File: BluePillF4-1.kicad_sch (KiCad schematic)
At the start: 57 parts, among them J1 MH20-1, J2 MH20-1, J3 MH_RA4-1, J4 47309-2651, J5 U02-BFD3111B0-009, U3 STM32F405RGT6, U4 SY6280, Y1 FC-12M, Y2 NX3225GD

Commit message: Removed unnecessary components like LiPo charger and fixed most errors. First connections between LoRa module and MCU created in the schematic.
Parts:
- removed R20: 0R, BluePillF4 Lib:R0603, symbol BluePillF4:RES_0603
- removed R21, R22: 10k, BluePillF4 Lib:R0603, symbol BluePillF4:RES_0603
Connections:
- net +VBAT is gone; now on net +3V3: J3.4
- net +3V3: now also J2.1
- net +3V3A: no longer J2.1
- net PA4 renamed LoRa_NSS
- net PA5 renamed LoRa_SCK
- net PA6 renamed LoRa_MISO
- net PA7 renamed LoRa_MOSI
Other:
- note removed: "Note: Mount L1 or U2, but not both"
- note removed: "VOLTAGE SENSE"

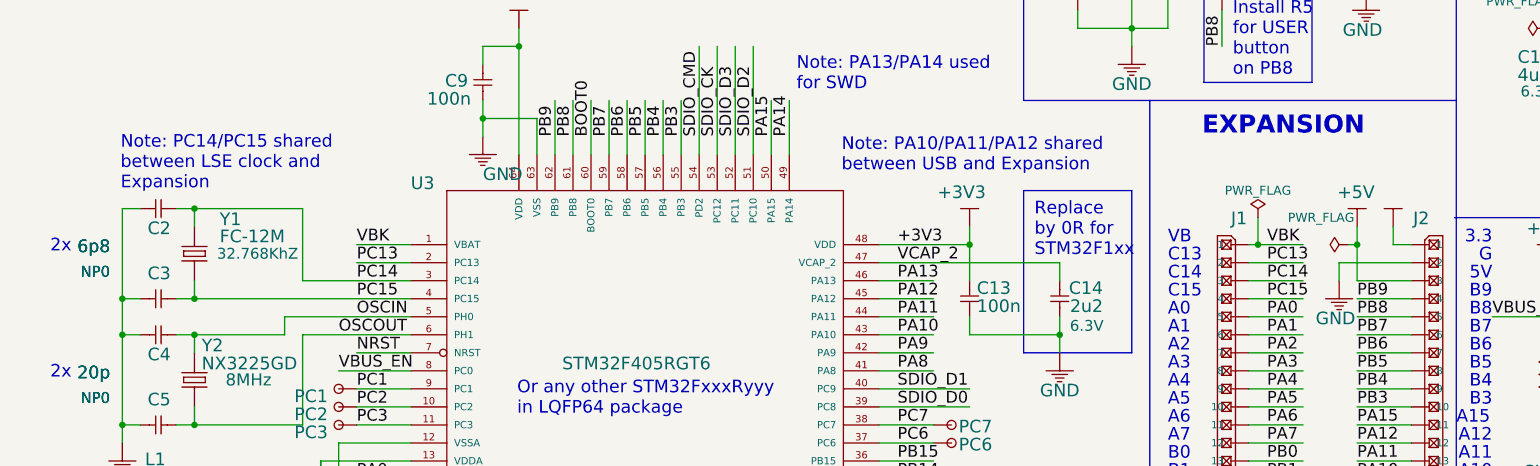
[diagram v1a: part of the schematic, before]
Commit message: Delete the RTC oscillator. First routing of the LoRa module.
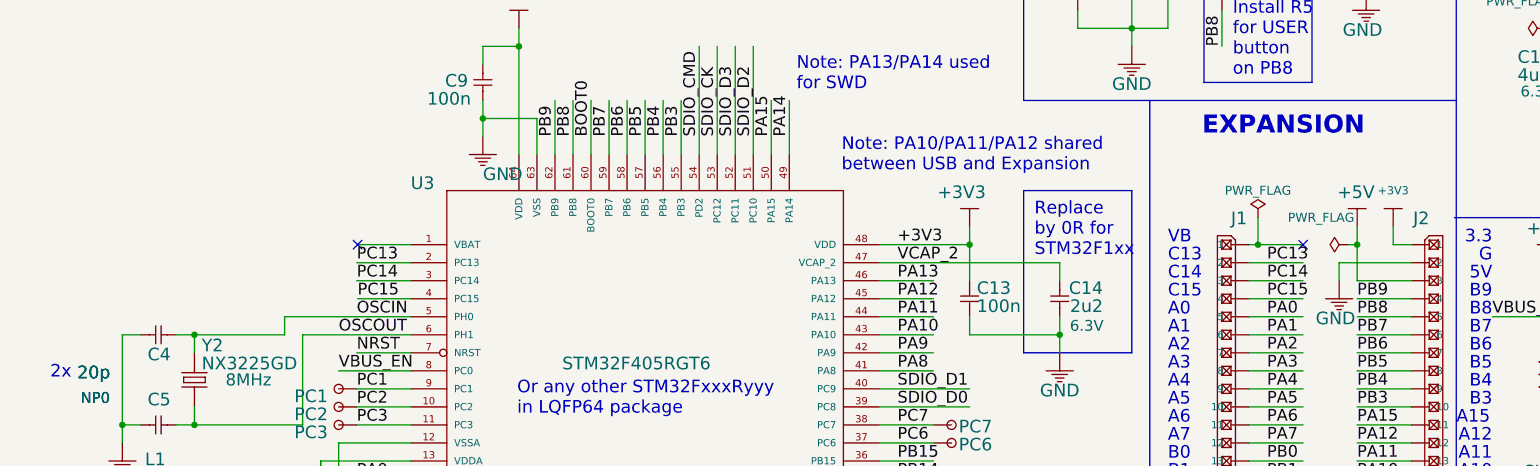
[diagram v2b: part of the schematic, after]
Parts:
- removed C2, C3: 6p8, BluePillF4 Lib:C0603, symbol BluePillF4:CAP_0603
- removed Y1: FC-12M, BluePillF4 Lib:FC-12M, symbol BluePillF4:FC-12M
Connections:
- net VBK: no longer names the net of J1.1
- net VBK: no longer U3.1 (VBAT)
- no-connect marks 6 -> 8
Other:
- note removed: "Note: PC14/PC15 shared between LSE clock and Expansion"
